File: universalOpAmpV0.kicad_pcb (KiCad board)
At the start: 6 copper layers, 0 parts

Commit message: Initial PCB layout
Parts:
- added C1: C, uniOpAmpLib:C_0805_Metric2012_HandSolder, B.Cu at (128.3, 112.4)
- added C2: C, uniOpAmpLib:C_0805_Metric2012_HandSolder, B.Cu at (120.5, 112.5)
- added C3: C, uniOpAmpLib:C_0805_Metric2012_HandSolder, B.Cu at (128.3, 110.4)
- added C4: C, uniOpAmpLib:C_0805_Metric2012_HandSolder, B.Cu at (118.5, 112.5)
- added C5: C, uniOpAmpLib:C_0805_Metric2012_HandSolder, B.Cu at (128.3, 108.4)
- added C6: C, uniOpAmpLib:C_0805_Metric2012_HandSolder, B.Cu at (116.5, 112.5)
- added C7: C_Small, uniOpAmpLib:PP_CAP, F.Cu at (100.9, 105.9)
- added C8: C_Small, uniOpAmpLib:PP_CAP, F.Cu at (105.6, 105.9)
- added C9: C_Small, uniOpAmpLib:PP_CAP, F.Cu at (111.9, 105.9)
- added D1: 1N4148WS, Diode_SMD:D_SOD-323, B.Cu at (124.0, 114.7)
- added RV1: R_Trim_Pot, uniOpAmpLib:PVG5H, F.Cu at (119.4, 108.5)
- added RV2: R_Trim_Pot, uniOpAmpLib:PVG5H, F.Cu at (119.4, 104.0)
- added SW3: 218-4LPSTR, uniOpAmpLib:218-4LPSTR, F.Cu at (124.1, 114.4)
- added SW4: SW_DPDT, uniOpAmpLib:CAS-DxxB, F.Cu at (115.5, 114.2)
- added SW5: SW_DPDT, uniOpAmpLib:CAS-DxxB, F.Cu at (109.5, 114.2)
- added SW6: CS-4-14, uniOpAmpLib:CS-4-14NB, F.Cu at (101.7, 113.6)
- added SW7: SW_SP3T, uniOpAmpLib:CS-4-13NB, F.Cu at (125.9, 106.0)
- added SW8: 218-8LPSTR, uniOpAmpLib:218-8LPSTR, F.Cu at (134.4, 110.3)
- added U1: OPA992DBV, uniOpAmpLib:SOT-23-5_HandSoldering, B.Cu at (124.0, 111.5)
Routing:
- net Net-(C7-Pad1): track 0.00 -> 42.0 mm
- net Net-(U1A--): track 0.00 -> 23.4 mm, vias 0 -> 1
- net A1: track 0.00 -> 21.1 mm, vias 0 -> 1
- net Net-(U1A-+): track 0.00 -> 18.3 mm, vias 0 -> 1
- net Net-(RV2-Pad1): track 0.00 -> 13.1 mm
- net Net-(RV1-Pad1): track 0.00 -> 12.9 mm
- net N1: track 0.00 -> 12.7 mm, vias 0 -> 2
- net Net-(SW5-B-Pad2): track 0.00 -> 10.7 mm
- net Net-(C9-Pad2): track 0.00 -> 9.93 mm
- net Net-(RV2-Pad3): track 0.00 -> 8.73 mm
- net Net-(SW3B-O): track 0.00 -> 7.80 mm
- net -VDC: track 0.00 -> 6.29 mm
- net Net-(SW3C-O): track 0.00 -> 6.24 mm
- net +VDC: track 0.00 -> 5.93 mm
- net Net-(D1-A): track 0.00 -> 5.67 mm, vias 0 -> 1
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- added copper zone on B.Cu, net GND
- added copper zone on F.Cu, net GND
- added copper zone on In1.Cu, net GND
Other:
- copper layers 6 -> 4

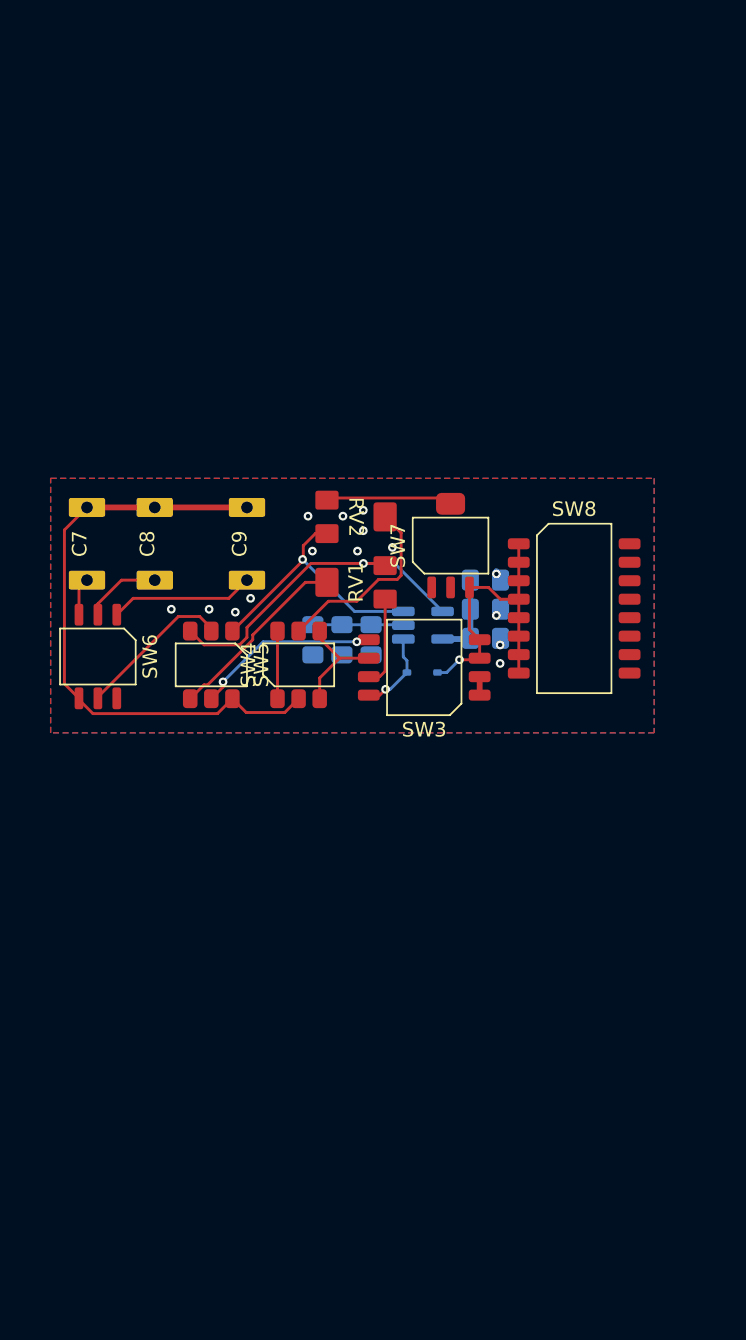
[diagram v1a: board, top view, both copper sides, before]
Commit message: critical fix to DPDT switch footprint pin numbering
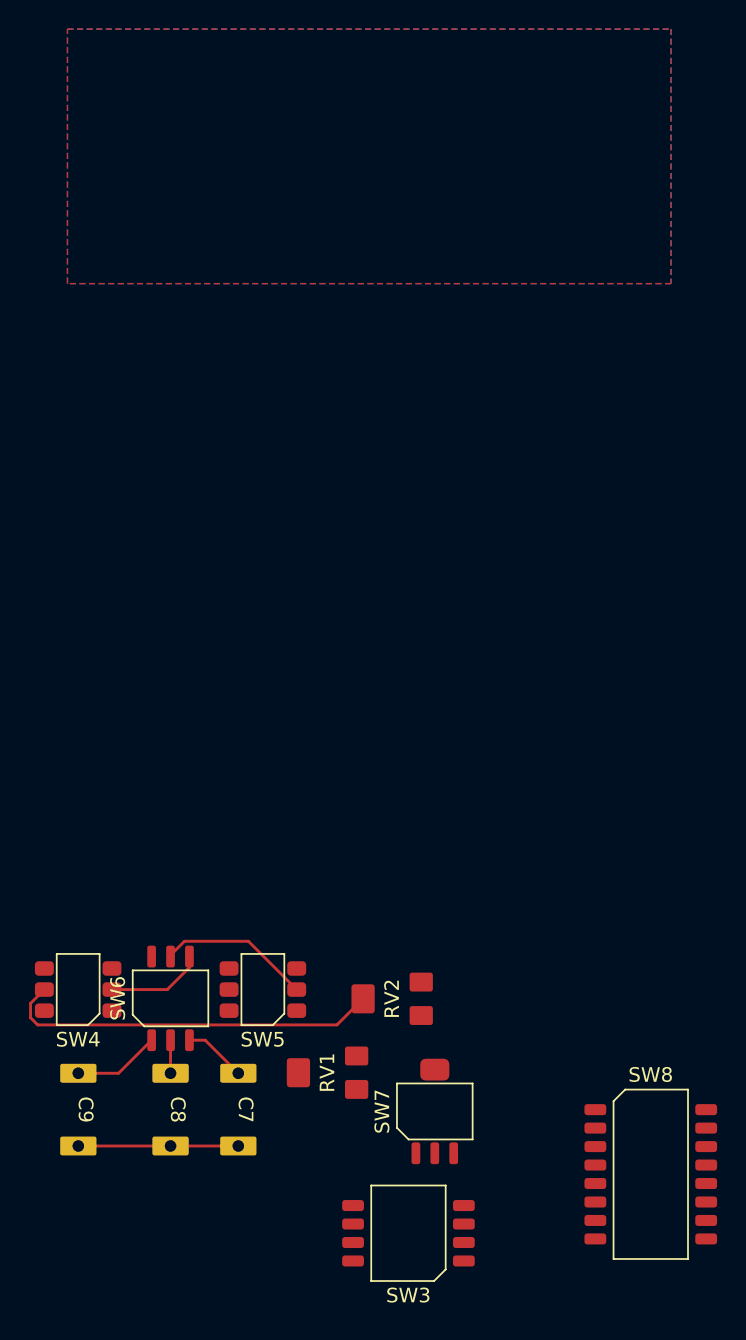
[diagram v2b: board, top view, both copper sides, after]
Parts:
- removed C1, C2, C3, C4, C5, C6: C, uniOpAmpLib:C_0805_Metric2012_HandSolder
- removed D1: 1N4148WS, Diode_SMD:D_SOD-323
- removed U1: OPA992DBV, uniOpAmpLib:SOT-23-5_HandSoldering
- moved C9 40.6 mm to (100.3, 144.8), turned to -90 degrees
- moved C7 40.3 mm to (111.3, 144.8), turned to -90 degrees
- moved SW8 39.3 mm to (139.7, 149.2)
- moved C8 38.9 mm to (106.7, 144.8), turned to -90 degrees
- moved SW3 38.9 mm to (123.0, 153.3)
- moved SW7 38.9 mm to (124.8, 144.9)
- moved RV1 33.8 mm to (117.5, 142.2)
- moved RV2 33.2 mm to (121.9, 137.2), turned to 90 degrees
- moved SW4 27.0 mm to (100.3, 136.5), turned to 90 degrees
- moved SW6 24.0 mm to (106.7, 137.1), turned to 0 degrees
- moved SW5 22.6 mm to (113.0, 136.5), turned to 90 degrees
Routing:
- net Net-(C7-Pad1): track 42.0 -> 17.7 mm
- net Net-(U1A--): track 23.4 -> 0.00 mm, vias 1 -> 0
- net A1: track 21.1 -> 0.00 mm, vias 1 -> 0
- net Net-(U1A-+): track 18.3 -> 0.00 mm, vias 1 -> 0
- net Net-(RV2-Pad1): track 13.1 -> 26.1 mm
- net Net-(RV1-Pad1): track 12.9 -> 0.00 mm
- net N1: track 12.7 -> 0.00 mm, vias 2 -> 0
- net Net-(RV2-Pad3): track 8.73 -> 0.00 mm
- net Net-(SW3B-O): track 7.80 -> 0.00 mm
- net -VDC: track 6.29 -> 0.00 mm
- net Net-(SW3C-O): track 6.24 -> 0.00 mm
- net +VDC: track 5.93 -> 0.00 mm
- net Net-(D1-A): track 5.67 -> 0.00 mm, vias 1 -> 0
- net P1: track 4.65 -> 0.00 mm
- net Net-(C9-Pad2): track 9.93 -> 5.98 mm
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
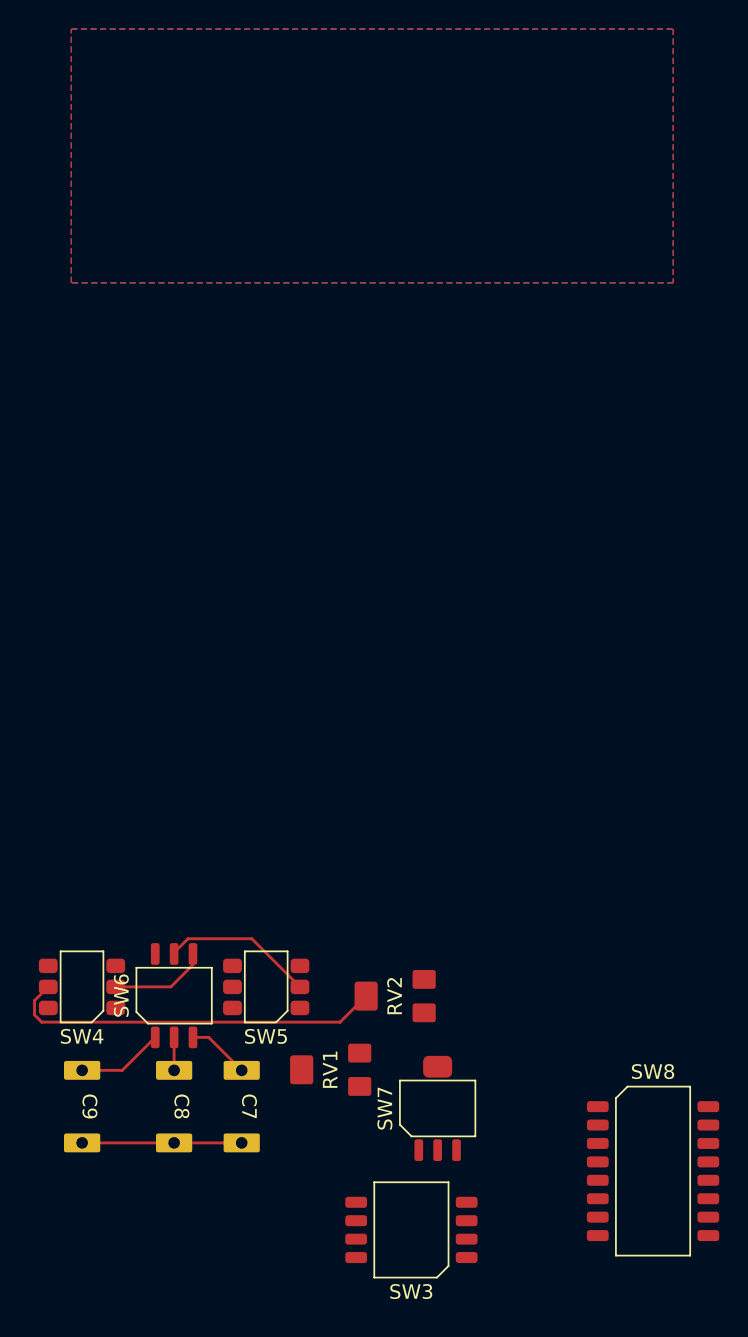
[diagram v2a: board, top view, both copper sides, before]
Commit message: improved op amp block layout
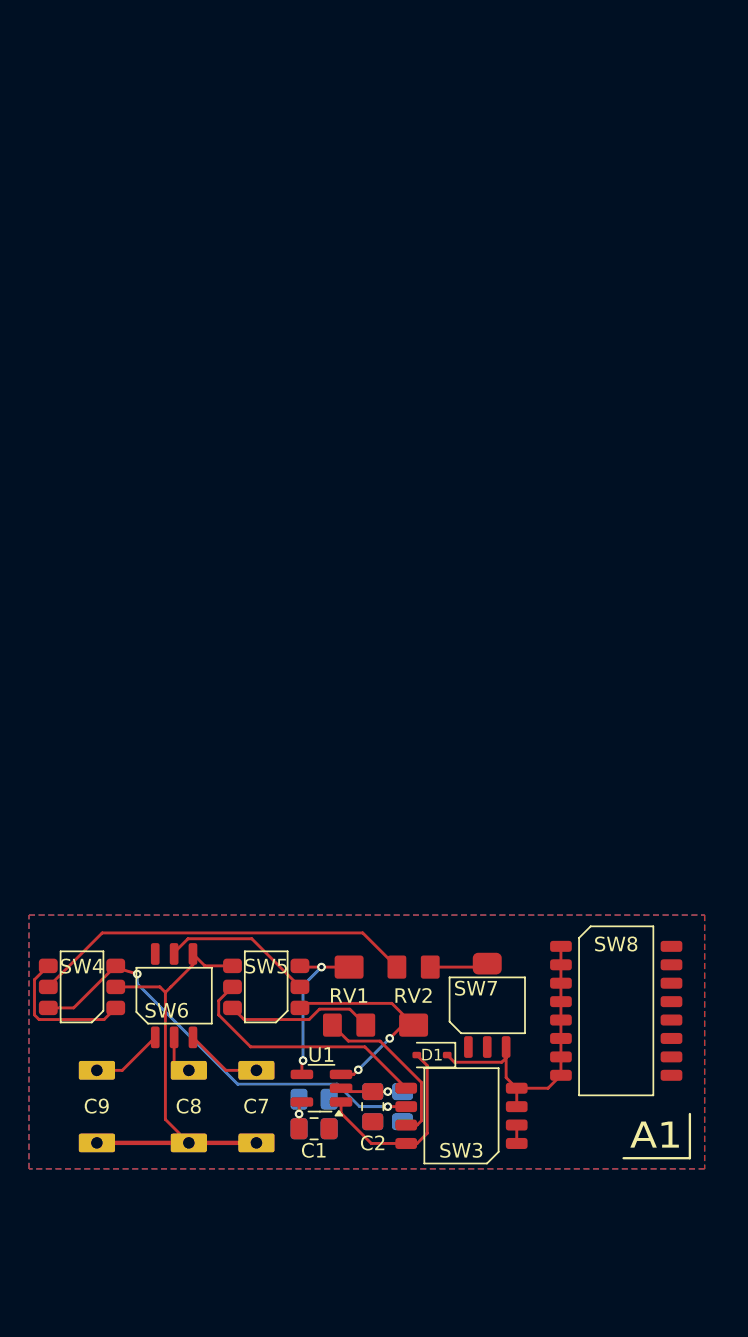
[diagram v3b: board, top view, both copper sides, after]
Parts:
- added C1: C, uniOpAmpLib:C_0805_Metric2012_HandSolder, F.Cu at (116.3, 146.3)
- added C2: C, uniOpAmpLib:C_0805_Metric2012_HandSolder, F.Cu at (120.4, 144.8)
- added C3: C, uniOpAmpLib:C_0805_Metric2012_HandSolder, B.Cu at (116.3, 144.3)
- added C4: C, uniOpAmpLib:C_0805_Metric2012_HandSolder, B.Cu at (120.4, 144.8)
- added C5: C, uniOpAmpLib:C_0805_Metric2012_HandSolder, B.Cu at (116.3, 146.3)
- added C6: C, uniOpAmpLib:C_0805_Metric2012_HandSolder, B.Cu at (122.4, 144.8)
- added D1: 1N4148WS, Diode_SMD:D_SOD-323, F.Cu at (124.5, 141.2)
- added U1: OPA992DBV, uniOpAmpLib:SOT-23-5_HandSoldering, F.Cu at (116.8, 143.5)
- moved SW8 11.3 mm to (137.2, 138.2)
- moved SW3 8.59 mm to (126.5, 145.4)
- moved SW7 7.89 mm to (128.3, 137.8)
- moved RV1 5.24 mm to (118.7, 137.2), turned to 0 degrees
- moved RV2 1.27 mm to (123.2, 137.2), turned to 180 degrees
- moved C7 1.02 mm to (112.4, 144.8)
- moved C8 1.02 mm to (107.7, 144.8)
- moved C9 1.02 mm to (101.4, 144.8)
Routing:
- net Net-(SW3B-O): track 0.00 -> 30.4 mm, vias 0 -> 2
- net A1: track 0.00 -> 21.9 mm
- net N1: track 0.00 -> 17.3 mm
- net Net-(U1A-+): track 0.00 -> 15.0 mm, vias 0 -> 2
- net Net-(C7-Pad1): track 17.7 -> 32.1 mm
- net Net-(D1-A): track 0.00 -> 13.6 mm
- net Net-(SW3C-O): track 0.00 -> 11.6 mm
- net Net-(U1A--): track 0.00 -> 11.4 mm, vias 0 -> 2
- net Net-(RV1-Pad1): track 0.00 -> 10.3 mm
- net P1: track 0.00 -> 9.84 mm
- net -VDC: track 0.00 -> 6.14 mm, vias 0 -> 1
- net Net-(RV2-Pad3): track 0.00 -> 4.03 mm
- net +VDC: track 0.00 -> 3.96 mm, vias 0 -> 1
- net GND: track 0.00 -> 1.27 mm
- net Net-(C7-Pad2): track 4.30 -> 5.32 mm
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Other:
- board text added: "A1"
